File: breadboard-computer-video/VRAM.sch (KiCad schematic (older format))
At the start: 8 parts

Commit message: fixed labels
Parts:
- gave numbers to parts that had none: 8
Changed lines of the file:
@@
 	1750 4600 2550 4600
 $Comp
-L 74xx:74LS245 U?
+L 74xx:74LS245 U45
 U 1 1 5E4F0138
 P 9450 5100
-F 0 "U?" H 9450 6081 50  0000 C CNN
+F 0 "U45" H 9450 6081 50  0000 C CNN
 F 1 "74LS245" H 9450 5990 50  0000 C CNN
 F 2 "" H 9450 5100 50  0001 C CNN
@@
 $EndComp
 $Comp
-L 74xx:74LS245 U?
+L 74xx:74LS245 U40
 U 1 1 5E500308
 P 3250 5300
-F 0 "U?" H 3250 6281 50  0000 C CNN
+F 0 "U40" H 3250 6281 50  0000 C CNN
 F 1 "74LS245" H 3250 6190 50  0000 C CNN
 F 2 "" H 3250 5300 50  0001 C CNN
@@
 $EndComp
 $Comp
-L 74xx:74LS243 U?
+L 74xx:74LS243 U39
 U 1 1 5E50F6D7
 P 3250 3550
-F 0 "U?" H 3250 4331 50  0000 C CNN
+F 0 "U39" H 3250 4331 50  0000 C CNN
 F 1 "74LS243" H 3250 4240 50  0000 C CNN
 F 2 "" H 3250 3550 50  0001 C CNN
@@
 	7650 4150 7650 5300
 $Comp
-L 74xx:74LS245 U?
+L 74xx:74LS245 U44
 U 1 1 5E4F9F1D
 P 7850 3650
-F 0 "U?" V 7804 4494 50  0000 L CNN
+F 0 "U44" V 7804 4494 50  0000 L CNN
 F 1 "74LS245" V 7895 4494 50  0000 L CNN
 F 2 "" H 7850 3650 50  0001 C CNN
@@
 	8150 4800 8950 4800
 $Comp
-L 74xx:74LS245 U?
+L 74xx:74LS245 U41
 U 1 1 5E55F96C
 P 4400 2500
-F 0 "U?" V 4354 3344 50  0000 L CNN
+F 0 "U41" V 4354 3344 50  0000 L CNN
 F 1 "74LS245" V 4445 3344 50  0000 L CNN
 F 2 "" H 4400 2500 50  0001 C CNN
@@
 	4200 5500 3750 5500
 $Comp
-L 74xx:74LS243 U?
+L 74xx:74LS243 U42
 U 1 1 5E57E59D
 P 6150 3100
-F 0 "U?" V 6104 3744 50  0000 L CNN
+F 0 "U42" V 6104 3744 50  0000 L CNN
 F 1 "74LS243" V 6195 3744 50  0000 L CNN
 F 2 "" H 6150 3100 50  0001 C CNN
@@
 Connection ~ 1200 3750
 $Comp
-L 74xx:74LS04 U?
+L 74xx:74LS04 U38
 U 1 1 5E788D2E
 P 2850 1800
-F 0 "U?" H 2850 2117 50  0000 C CNN
+F 0 "U38" H 2850 2117 50  0000 C CNN
 F 1 "74LS04" H 2850 2026 50  0000 C CNN
 F 2 "" H 2850 1800 50  0001 C CNN
@@
 	1200 850  1200 1800
 $Comp
-L Memory_RAM:628128_DIP32_SSOP32 U?
+L Memory_RAM:628128_DIP32_SSOP32 U43
 U 1 1 5E7988CF
 P 6250 5400
-F 0 "U?" H 6250 6581 50  0000 C CNN
+F 0 "U43" H 6250 6581 50  0000 C CNN
 F 1 "628128_DIP32_SSOP32" H 6250 6490 50  0000 C CNN
 F 2 "" H 6250 5400 50  0001 C CNN

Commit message: switched to active high
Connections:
- wire segments 184 -> 190
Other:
- note added: "Write (Active Low)"
- note removed: "Write (Active High)"
- moved on the sheet: U38A
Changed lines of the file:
@@
 Wire Wire Line
 	6350 3600 6350 3850
-Wire Wire Line
-	4200 2000 4200 850
-Wire Wire Line
-	4300 2000 4300 850
-Wire Wire Line
-	4400 2000 4400 850
-Wire Wire Line
-	4500 2000 4500 850
-Wire Wire Line
-	4600 2000 4600 850
-Wire Wire Line
-	4700 2000 4700 850
-Wire Wire Line
-	4800 2000 4800 850
-Wire Wire Line
-	4900 2000 4900 850
 NoConn ~ 6250 2600
 NoConn ~ 6150 2600
@@
 Wire Wire Line
 	5350 4300 6250 4300
-Wire Wire Line
-	7650 850  7650 3150
-Wire Wire Line
-	7750 850  7750 3150
-Wire Wire Line
-	7850 850  7850 3150
-Wire Wire Line
-	7950 850  7950 3150
-Wire Wire Line
-	8050 850  8050 3150
-Wire Wire Line
-	8150 850  8150 3150
-Wire Wire Line
-	8250 850  8250 3150
-Wire Wire Line
-	8350 850  8350 3150
 $Comp
 L power:Earth #PWR?
@@
 	3900 2000 3900 1800
 Wire Wire Line
-	3900 1800 3150 1800
-Wire Wire Line
 	5950 2600 5950 1800
 Wire Wire Line
@@
 L 74xx:74LS04 U38
 U 1 1 5E788D2E
-P 2850 1800
-F 0 "U38" H 2850 2117 50  0000 C CNN
-F 1 "74LS04" H 2850 2026 50  0000 C CNN
-F 2 "" H 2850 1800 50  0001 C CNN
-F 3 "http://www.ti.com/lit/gpn/sn74LS04" H 2850 1800 50  0001 C CNN
-	1    2850 1800
-	1    0    0    -1
+P 1200 2700
+F 0 "U38" H 1200 3017 50  0000 C CNN
+F 1 "74LS04" H 1200 2926 50  0000 C CNN
+F 2 "" H 1200 2700 50  0001 C CNN
+F 3 "http://www.ti.com/lit/gpn/sn74LS04" H 1200 2700 50  0001 C CNN
+	1    1200 2700
+	0    1    1    0
 $EndComp
 Wire Wire Line
@@
 Wire Wire Line
 	7350 3050 7350 1800
-Wire Wire Line
-	2550 1800 1200 1800
 Connection ~ 1200 1800
 Wire Wire Line
-	1200 1800 1200 3750
-Wire Wire Line
-	5000 850  5000 1600
-Wire Wire Line
-	5000 1600 6350 1600
-Wire Wire Line
-	6350 1600 6350 2600
-Wire Wire Line
-	6450 1500 5100 1500
-Wire Wire Line
-	5100 1500 5100 850
-Wire Wire Line
-	6450 1500 6450 2600
+	1200 1800 1200 2400
 Text Notes 2000 1000 2    50   ~ 0
-Write (Active High)
-Text Notes 5700 1000 2    50   ~ 0
+Write (Active Low)
+Text Notes 10850 3900 2    50   ~ 0
 Address Input
-Text Notes 8850 1000 2    50   ~ 0
+Text Notes 10750 4050 2    50   ~ 0
 Data Input
+Wire Wire Line
+	7650 2500 7650 3150
+Wire Wire Line
+	7750 2500 7750 3150
+Wire Wire Line
+	7850 2500 7850 3150
+Wire Wire Line
+	7950 2500 7950 3150
+Wire Wire Line
+	8050 2500 8050 3150
+Wire Wire Line
+	8150 2500 8150 3150
+Wire Wire Line
+	8250 2500 8250 3150
+Wire Wire Line
+	8350 2500 8350 3150
+Wire Wire Line
+	4200 700  6850 700
+Wire Wire Line
+	4300 800  6850 800
+Wire Wire Line
+	4400 900  6850 900
+Wire Wire Line
+	4200 700  4200 2000
+Wire Wire Line
+	4300 800  4300 2000
+Wire Wire Line
+	4400 900  4400 2000
+Wire Wire Line
+	4500 1000 6850 1000
+Wire Wire Line
+	4500 1000 4500 2000
+Wire Wire Line
+	4600 1100 6850 1100
+Wire Wire Line
+	4600 1100 4600 2000
+Wire Wire Line
+	4700 1200 6850 1200
+Wire Wire Line
+	4700 1200 4700 2000
+Wire Wire Line
+	4800 1300 6850 1300
+Wire Wire Line
+	4800 1300 4800 2000
+Wire Wire Line
+	4900 1400 6850 1400
+Wire Wire Line
+	4900 1400 4900 2000
+Wire Wire Line
+	6350 1500 6350 2600
+Wire Wire Line
+	6450 1600 6850 1600
+Wire Wire Line
+	6450 1600 6450 2600
+Wire Wire Line
+	6350 1500 6850 1500
+Wire Wire Line
+	1200 3000 1200 3750
+Wire Wire Line
+	1200 1800 3900 1800
 $EndSCHEMATC

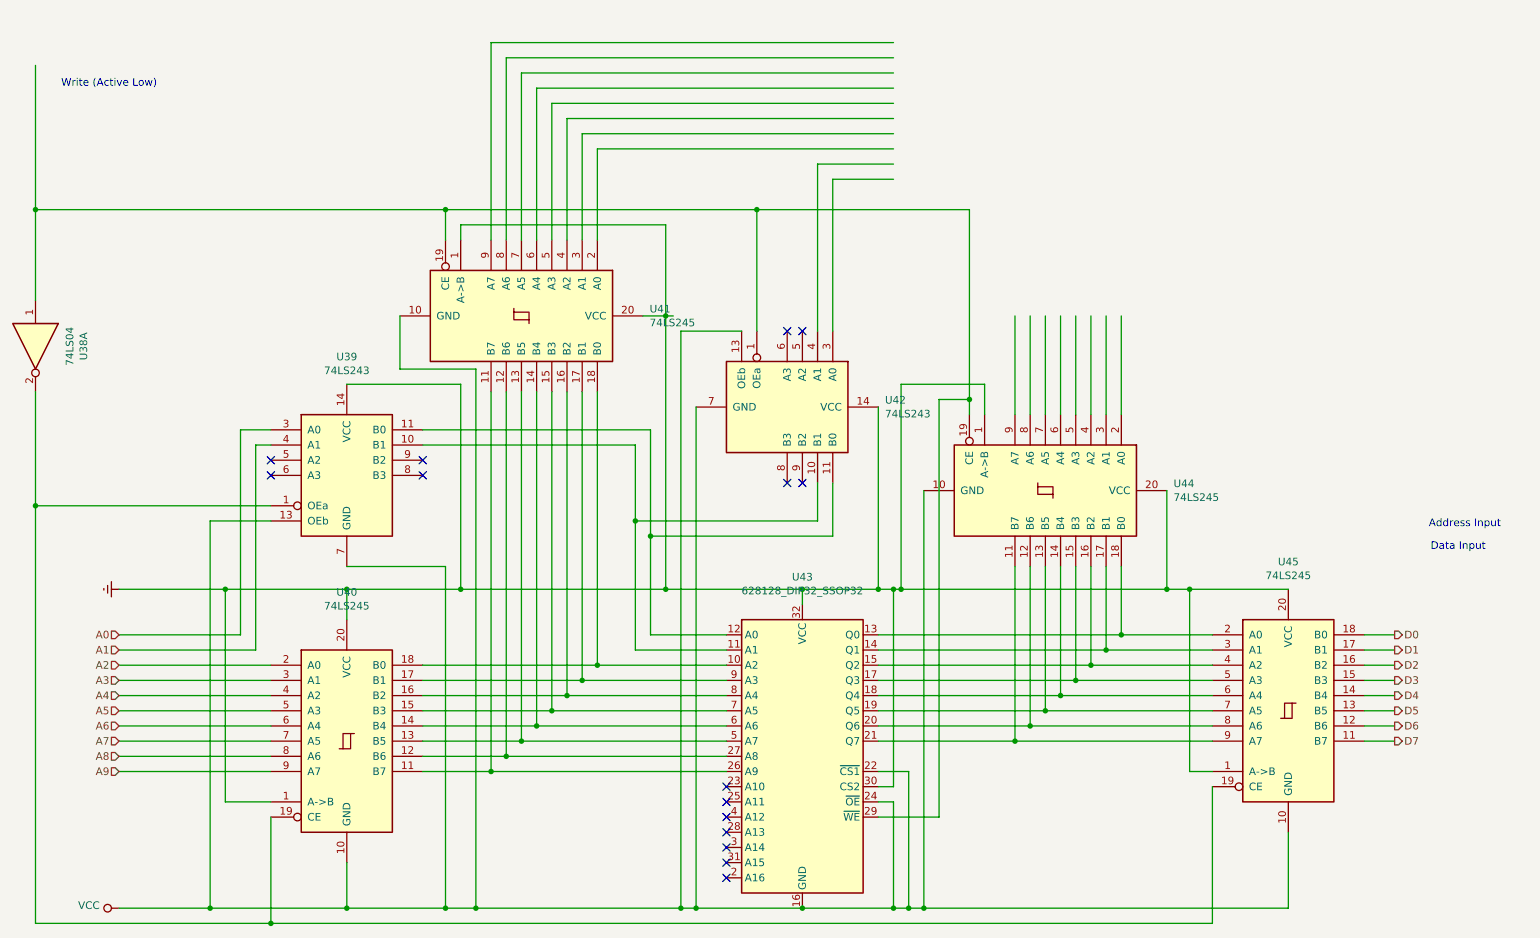
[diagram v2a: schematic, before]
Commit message: added vram data register
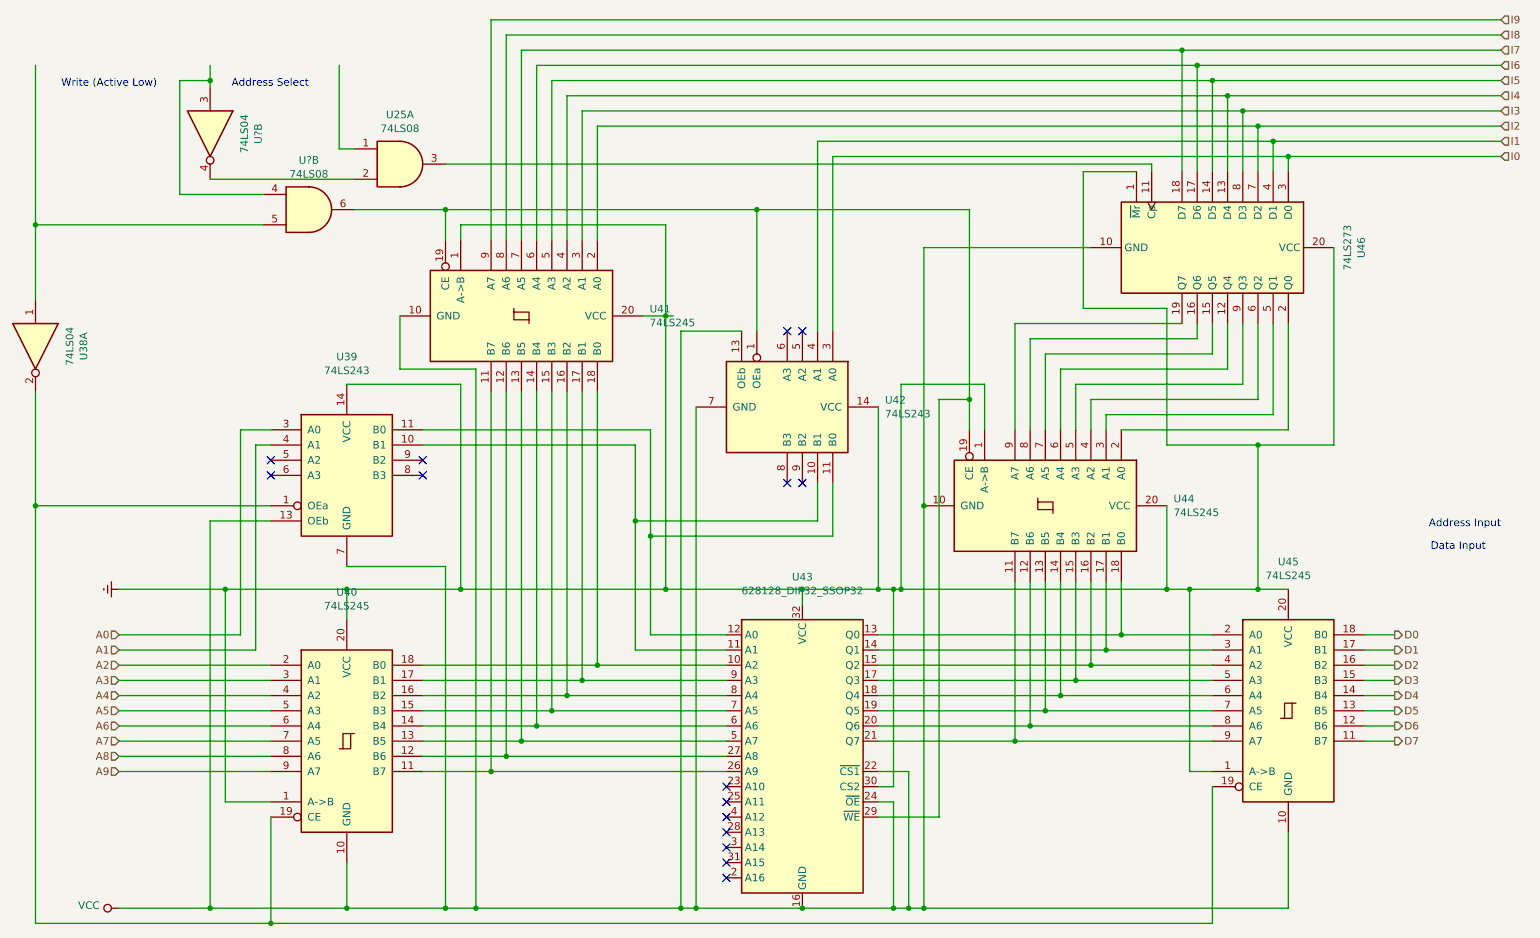
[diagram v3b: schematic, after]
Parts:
- added U25, U?: 74LS08, symbol 74xx:74LS08
- added U46: 74LS273, symbol 74xx:74LS273
- added U?: 74LS04, symbol 74xx:74LS04
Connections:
- net labels added: I0, I1, I2, I3, I4, I5, I6, I7, I8, I9
- wire segments 190 -> 242
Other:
- note added: "Address Select"
- moved on the sheet: U44

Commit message: finished hv sync
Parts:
- gave numbers to parts that had none: 2
- renumbered U25 to U37, U46 to U38, U41 to U39, U38 to U40, U42 to U41, U39 to U42, U44 to U43, U45 to U44, U40 to U45, U43 to U46
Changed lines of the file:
@@
 	1750 4600 2550 4600
 $Comp
-L 74xx:74LS245 U45
+L 74xx:74LS245 U44
 U 1 1 5E4F0138
 P 9450 5100
-F 0 "U45" H 9450 6081 50  0000 C CNN
+F 0 "U44" H 9450 6081 50  0000 C CNN
 F 1 "74LS245" H 9450 5990 50  0000 C CNN
 F 2 "" H 9450 5100 50  0001 C CNN
@@
 $EndComp
 $Comp
-L 74xx:74LS245 U40
+L 74xx:74LS245 U45
 U 1 1 5E500308
 P 3250 5300
-F 0 "U40" H 3250 6281 50  0000 C CNN
+F 0 "U45" H 3250 6281 50  0000 C CNN
 F 1 "74LS245" H 3250 6190 50  0000 C CNN
 F 2 "" H 3250 5300 50  0001 C CNN
@@
 $EndComp
 $Comp
-L 74xx:74LS243 U39
+L 74xx:74LS243 U42
 U 1 1 5E50F6D7
 P 3250 3550
-F 0 "U39" H 3250 4331 50  0000 C CNN
+F 0 "U42" H 3250 4331 50  0000 C CNN
 F 1 "74LS243" H 3250 4240 50  0000 C CNN
 F 2 "" H 3250 3550 50  0001 C CNN
@@
 	7650 4250 7650 5300
 $Comp
-L 74xx:74LS245 U44
+L 74xx:74LS245 U43
 U 1 1 5E4F9F1D
 P 7850 3750
-F 0 "U44" V 7804 4594 50  0000 L CNN
+F 0 "U43" V 7804 4594 50  0000 L CNN
 F 1 "74LS245" V 7895 4594 50  0000 L CNN
 F 2 "" H 7850 3750 50  0001 C CNN
@@
 	8150 4800 8950 4800
 $Comp
-L 74xx:74LS245 U41
+L 74xx:74LS245 U39
 U 1 1 5E55F96C
 P 4400 2500
-F 0 "U41" V 4354 3344 50  0000 L CNN
+F 0 "U39" V 4354 3344 50  0000 L CNN
 F 1 "74LS245" V 4445 3344 50  0000 L CNN
 F 2 "" H 4400 2500 50  0001 C CNN
@@
 	4200 5500 3750 5500
 $Comp
-L 74xx:74LS243 U42
+L 74xx:74LS243 U41
 U 1 1 5E57E59D
 P 6150 3100
-F 0 "U42" V 6104 3744 50  0000 L CNN
+F 0 "U41" V 6104 3744 50  0000 L CNN
 F 1 "74LS243" V 6195 3744 50  0000 L CNN
 F 2 "" H 6150 3100 50  0001 C CNN
@@
 Connection ~ 1200 3750
 $Comp
-L 74xx:74LS04 U38
+L 74xx:74LS04 U40
 U 1 1 5E788D2E
 P 1200 2700
-F 0 "U38" H 1200 3017 50  0000 C CNN
+F 0 "U40" H 1200 3017 50  0000 C CNN
 F 1 "74LS04" H 1200 2926 50  0000 C CNN
 F 2 "" H 1200 2700 50  0001 C CNN
@@
 $EndComp
 $Comp
-L Memory_RAM:628128_DIP32_SSOP32 U43
+L Memory_RAM:628128_DIP32_SSOP32 U46
 U 1 1 5E7988CF
 P 6250 5400
-F 0 "U43" H 6250 6581 50  0000 C CNN
+F 0 "U46" H 6250 6581 50  0000 C CNN
 F 1 "628128_DIP32_SSOP32" H 6250 6490 50  0000 C CNN
 F 2 "" H 6250 5400 50  0001 C CNN
@@
 	9050 2550 9050 2850
 $Comp
-L 74xx:74LS273 U46
+L 74xx:74LS273 U38
 U 1 1 5DC9EF95
 P 8950 2050
-F 0 "U46" H 8950 3031 50  0000 C CNN
+F 0 "U38" H 8950 3031 50  0000 C CNN
 F 1 "74LS273" H 8950 2940 50  0000 C CNN
 F 2 "" H 8950 2050 50  0001 C CNN
@@
 Connection ~ 9250 3350
 $Comp
-L 74xx:74LS08 U25
+L 74xx:74LS08 U37
 U 1 1 5E12CF66
 P 3600 1500
-F 0 "U25" H 3600 1825 50  0000 C CNN
+F 0 "U37" H 3600 1825 50  0000 C CNN
 F 1 "74LS08" H 3600 1734 50  0000 C CNN
 F 2 "" H 3600 1500 50  0001 C CNN
@@
 	3200 1400 3200 850
 $Comp
-L 74xx:74LS04 U?
+L 74xx:74LS04 U36
 U 2 1 5E18D583
 P 2350 1300
-F 0 "U?" H 2350 1617 50  0000 C CNN
+F 0 "U36" H 2350 1617 50  0000 C CNN
 F 1 "74LS04" H 2350 1526 50  0000 C CNN
 F 2 "" H 2350 1300 50  0001 C CNN
@@
 	2350 1600 3300 1600
 $Comp
-L 74xx:74LS08 U?
+L 74xx:74LS08 U15
 U 2 1 5E1EAD04
 P 3000 1800
-F 0 "U?" H 3000 2125 50  0000 C CNN
+F 0 "U15" H 3000 2125 50  0000 C CNN
 F 1 "74LS08" H 3000 2034 50  0000 C CNN
 F 2 "" H 3000 1800 50  0001 C CNN
